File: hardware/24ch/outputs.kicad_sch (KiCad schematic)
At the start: 41 parts, among them J701 TRIP C-NO-NC, J702 ALM C-NO-NC, J703 RS485 A B GND, K701 G6K-2F-Y DC5, K702 G6K-2F-Y DC5, Q701 2N7002, Q702 2N7002, U703 ADM2587EBRWZ

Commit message: 24ch cheaper-parts variant (0036): TMP126, CA-IS3761HW, RS-485 DNP, drop-in swaps
- CJ sensors ADT7310 x6 -> TMP126DCKR (C5219998); R443 22k DIN_ISO-DOUT_ISO for the
  3-wire SIO, R415 removed, ALERT grounded. Sensors moved <= 8 mm to clear spots beside
  their 100 nF (no closer spot to the terminals without touching TC traces, 0035 D2).
- ISO7761 -> CA-IS3761HW (same pinout, 5F/1R, default high); BOCHEN 3296W trimmer;
  SAMWHA 22u 1210.
- RS-485 block DNP: footprints kept; fab.py drops DNP parts from BOM/CPL and writes
  DNP.txt; cost.py skips them. External window watchdog tried and removed (owner).
- gen/delta.py: carry a schematic change onto the routed board (replace/add/remove,
  re-net, DNP, OLD>NEW@DEG reuse); it never deletes another net's track under a pad.
- Board: incremental edits only; analog nets (TC*, V_BIAS, VREF, REF*) identical to
  the pre-0036 board. Gates: ERC 0/0 (471 symbols); fab.py DRC/unconnected/parity
  0/0/0; pincaps 0 over. Parts ~$105 -> ~$72/board (CALCULATIONS 8.1, by hand).
- Docs: decision 0036, CALCULATIONS 8, ISSUES (I-109, I-114, I-119, I-104, I-094,
  new I-123 stock), STATE, 24ch README, superseded.txt.

Co-Authored-By: Claude Opus 5.5 <noreply@anthropic.com>
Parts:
- C731, C732, C733, C734, C735, C736, D731, J703, JP731, JP732, JP733, R733, R734, R735, R736, U703: now not fitted
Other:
- note added: "Isolated RS-485 / Modbus RTU (never in the trip path) - DNP: footprints only, fit when a site needs it (0036)"
- note removed: "Isolated RS-485 / Modbus RTU (never in the trip path)"
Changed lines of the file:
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@@
 		)
 	)
-	(text "Isolated RS-485 / Modbus RTU (never in the trip path)"
+	(text "Isolated RS-485 / Modbus RTU (never in the trip path) - DNP: footprints only, fit when a site needs it (0036)"
 		(exclude_from_sim no)
 		(at 15 119.6124 0)
@@
 		(in_bom yes)
 		(on_board yes)
-		(dnp no)
+		(dnp yes)
 		(property "Reference" "U703"
 			(at 27.94 128.68 0)
@@
 		(in_bom yes)
 		(on_board yes)
-		(dnp no)
+		(dnp yes)
 		(property "Reference" "R733"
 			(at 78.016 141.24 0)
@@
 		(in_bom yes)
 		(on_board yes)
-		(dnp no)
+		(dnp yes)
 		(property "Reference" "C735"
 			(at 114.592 138.7 0)
@@
 		(in_bom yes)
 		(on_board yes)
-		(dnp no)
+		(dnp yes)
 		(property "Reference" "C736"
 			(at 129.832 141.24 0)
@@
 		(in_bom yes)
 		(on_board yes)
-		(dnp no)
+		(dnp yes)
 		(property "Reference" "C731"
 			(at 142.532 138.7 0)
@@
 		(in_bom yes)
 		(on_board yes)
-		(dnp no)
+		(dnp yes)
 		(property "Reference" "C732"
 			(at 157.772 138.7 0)
@@
 		(in_bom yes)
 		(on_board yes)
-		(dnp no)
+		(dnp yes)
 		(property "Reference" "C733"
 			(at 170.472 141.24 0)
@@
 		(in_bom yes)
 		(on_board yes)
-		(dnp no)
+		(dnp yes)
 		(property "Reference" "C734"
 			(at 183.172 141.24 0)
@@
 		(in_bom yes)
 		(on_board yes)
-		(dnp no)
+		(dnp yes)
 		(property "Reference" "D731"
 			(at 201.93 129.95 0)
@@
 		(in_bom yes)
 		(on_board yes)
-		(dnp no)
+		(dnp yes)
 		(property "Reference" "JP731"
 			(at 253.53 126 0)
@@
 		(in_bom yes)
 		(on_board yes)
-		(dnp no)
+		(dnp yes)
 		(property "Reference" "R734"
 			(at 265.976 141.24 0)
@@
 		(in_bom yes)
 		(on_board yes)
-		(dnp no)
+		(dnp yes)
 		(property "Reference" "JP732"
 			(at 296.71 126 0)
@@
 		(in_bom yes)
 		(on_board yes)
-		(dnp no)
+		(dnp yes)
 		(property "Reference" "R735"
 			(at 311.696 141.24 0)
@@
 		(in_bom yes)
 		(on_board yes)
-		(dnp no)
+		(dnp yes)
 		(property "Reference" "JP733"
 			(at 342.43 126 0)
@@
 		(in_bom yes)
 		(on_board yes)
-		(dnp no)
+		(dnp yes)
 		(property "Reference" "R736"
 			(at 354.876 141.24 0)
@@
 		(in_bom yes)
 		(on_board yes)
-		(dnp no)
+		(dnp yes)
 		(property "Reference" "J703"
 			(at 385.61 128.54 0)

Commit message: 24ch 0036 D7/D8: screw terminals face the board edge; supplier files as an RFQ
- J601/J701/J702/J703 turned 180 deg about the middle pin (wire entry was blocked by the
  relays ~2 mm in front); pin numbers 1<->3 swapped in the generator so every position keeps
  its net, label and copper. RS-485 row (DNP) moved 0.5 mm with its track ends, BIAS_B routed
  around J703 pin 1, TRIP_COM stub extended to the round pad.
- delta.py: MPN/LCSC/Manufacturer fields go to F.Fab hidden (were printed on the silkscreen of
  the six TMP126), new footprints hide reference/value like the rest of the board.
- fab.py: ORDER-NOTES rewritten as a friendly request for quotation (LCSC = reference only,
  equivalents welcome, preferences not conditions, terminal direction named); BOM.csv/CPL.csv;
  supplier ACCESSORIES.csv without internal notes or RS-485 items.
- Gates: ERC 0/0; DRC 0 violations / 0 unconnected; pincaps 0 over; analog nets identical to
  the pre-0036 board.

Co-Authored-By: Claude Opus 5.5 <noreply@anthropic.com>
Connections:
- net ALM_COM: now also J702.3 (Pin_3); no longer J702.1 (Pin_1)
- net ALM_NC: now also J702.1 (Pin_1); no longer J702.3 (Pin_3)
- net GND_RS485: now also J703.1 (Pin_1); no longer J703.3 (Pin_3)
- net RS485_A: now also J703.3 (Pin_3); no longer J703.1 (Pin_1)
- net TRIP_COM: now also J701.3 (Pin_3); no longer J701.1 (Pin_1)
- net TRIP_NC: now also J701.1 (Pin_1); no longer J701.3 (Pin_3)
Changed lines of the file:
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@@
 		)
 	)
-	(label "TRIP_COM"
+	(label "TRIP_NC"
 		(at 294.64 27.94 180)
 		(effects
@@
 		)
 	)
-	(label "TRIP_NC"
+	(label "TRIP_COM"
 		(at 294.64 33.02 180)
 		(effects
@@
 		)
 	)
-	(label "ALM_COM"
+	(label "ALM_NC"
 		(at 223.52 78.74 180)
 		(effects
@@
 		)
 	)
-	(label "ALM_NC"
+	(label "ALM_COM"
 		(at 223.52 83.82 180)
 		(effects
@@
 		)
 	)
-	(label "RS485_A"
+	(label "GND_RS485"
 		(at 375.92 127 180)
 		(effects
@@
 		)
 	)
-	(label "GND_RS485"
+	(label "RS485_A"
 		(at 375.92 132.08 180)
 		(effects

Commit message: 24ch 0036 D9: RS-485/Modbus fitted again (owner), release tooling for no DNP
- c_out.py: the 16 RS-485 parts are fitted (reverses 0036 D2); build.py
  ERC 0/0, netlist check 0/0. delta.py cleared the 16 DNP flags on the
  board, no copper changed (0 tracks deleted); pincaps 0 over the limit.
- fab.py: DNP.txt says "none" when every footprint is fitted; jumper shunts
  for JP731-JP733 go to the supplier accessories; J703 in the terminal
  orientation note.
- assembly_spec.py: counts and the through-hole list read from BOM.csv;
  section 6 adapts to a release without DNP; U703 and J703 in the checklist.
- docs: 0036 D9, I-094, CALCULATIONS 8.1 (+$8.64/board).

Co-Authored-By: Claude Opus 5.5 <noreply@anthropic.com>
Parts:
- C731, C732, C733, C734, C735, C736, D731, J703, JP731, JP732, JP733, R733, R734, R735, R736, U703: now fitted
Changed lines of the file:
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@@
 		(in_bom yes)
 		(on_board yes)
-		(dnp yes)
+		(dnp no)
 		(property "Reference" "U703"
 			(at 27.94 128.68 0)
@@
 		(in_bom yes)
 		(on_board yes)
-		(dnp yes)
+		(dnp no)
 		(property "Reference" "R733"
 			(at 78.016 141.24 0)
@@
 		(in_bom yes)
 		(on_board yes)
-		(dnp yes)
+		(dnp no)
 		(property "Reference" "C735"
 			(at 114.592 138.7 0)
@@
 		(in_bom yes)
 		(on_board yes)
-		(dnp yes)
+		(dnp no)
 		(property "Reference" "C736"
 			(at 129.832 141.24 0)
@@
 		(in_bom yes)
 		(on_board yes)
-		(dnp yes)
+		(dnp no)
 		(property "Reference" "C731"
 			(at 142.532 138.7 0)
@@
 		(in_bom yes)
 		(on_board yes)
-		(dnp yes)
+		(dnp no)
 		(property "Reference" "C732"
 			(at 157.772 138.7 0)
@@
 		(in_bom yes)
 		(on_board yes)
-		(dnp yes)
+		(dnp no)
 		(property "Reference" "C733"
 			(at 170.472 141.24 0)
@@
 		(in_bom yes)
 		(on_board yes)
-		(dnp yes)
+		(dnp no)
 		(property "Reference" "C734"
 			(at 183.172 141.24 0)
@@
 		(in_bom yes)
 		(on_board yes)
-		(dnp yes)
+		(dnp no)
 		(property "Reference" "D731"
 			(at 201.93 129.95 0)
@@
 		(in_bom yes)
 		(on_board yes)
-		(dnp yes)
+		(dnp no)
 		(property "Reference" "JP731"
 			(at 253.53 126 0)
@@
 		(in_bom yes)
 		(on_board yes)
-		(dnp yes)
+		(dnp no)
 		(property "Reference" "R734"
 			(at 265.976 141.24 0)
@@
 		(in_bom yes)
 		(on_board yes)
-		(dnp yes)
+		(dnp no)
 		(property "Reference" "JP732"
 			(at 296.71 126 0)
@@
 		(in_bom yes)
 		(on_board yes)
-		(dnp yes)
+		(dnp no)
 		(property "Reference" "R735"
 			(at 311.696 141.24 0)
@@
 		(in_bom yes)
 		(on_board yes)
-		(dnp yes)
+		(dnp no)
 		(property "Reference" "JP733"
 			(at 342.43 126 0)
@@
 		(in_bom yes)
 		(on_board yes)
-		(dnp yes)
+		(dnp no)
 		(property "Reference" "R736"
 			(at 354.876 141.24 0)
@@
 		(in_bom yes)
 		(on_board yes)
-		(dnp yes)
+		(dnp no)
 		(property "Reference" "J703"
 			(at 385.61 128.54 0)

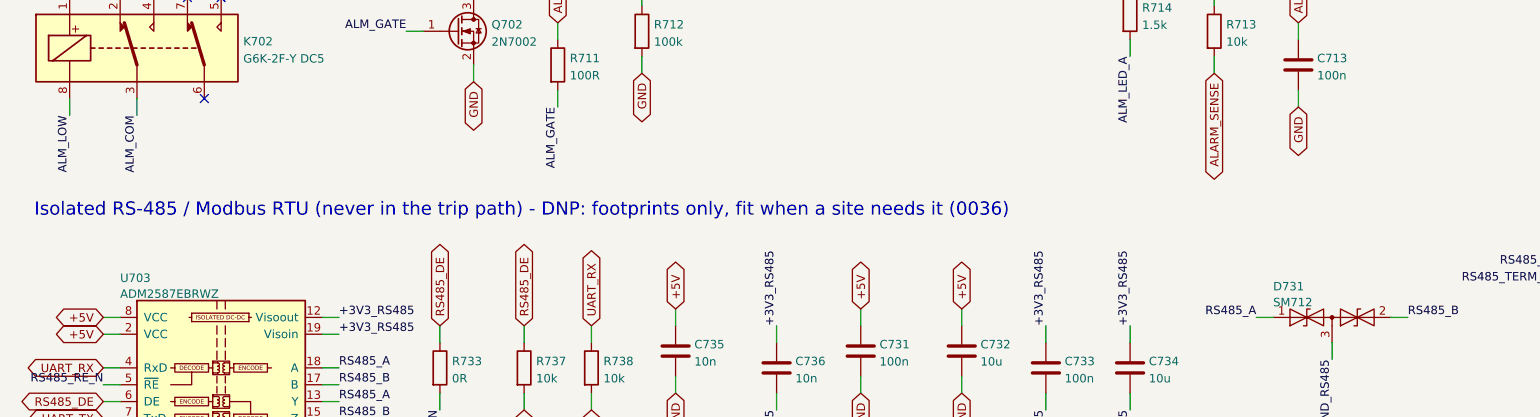
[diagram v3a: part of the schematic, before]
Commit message: 24ch REV A4: Astra review fixes, release 195548-b4c4e2
Astra (gpt-6-astra, high): no redesign blocker. Fixed its documentation
findings: schematic title REV A4 and RS-485 block no longer called DNP;
ASSEMBLY-SPEC.pdf generated into the release; I-085 now says J601 pin 1 =
CHASSIS, pin 3 = +24V (0036 D7 turn); TMP126 write transactions keep
SIO_WR_N low through data and CRC (0041, c_iso.py note).
ERC 0/0, netlist 0 mismatches, board unchanged (delta dry: 0), release DRC
0/0/0, BOM 96 lines. Previous releases archived in _OLD_DO_NOT_ORDER.

Co-Authored-By: Claude Opus 5.5 <noreply@anthropic.com>
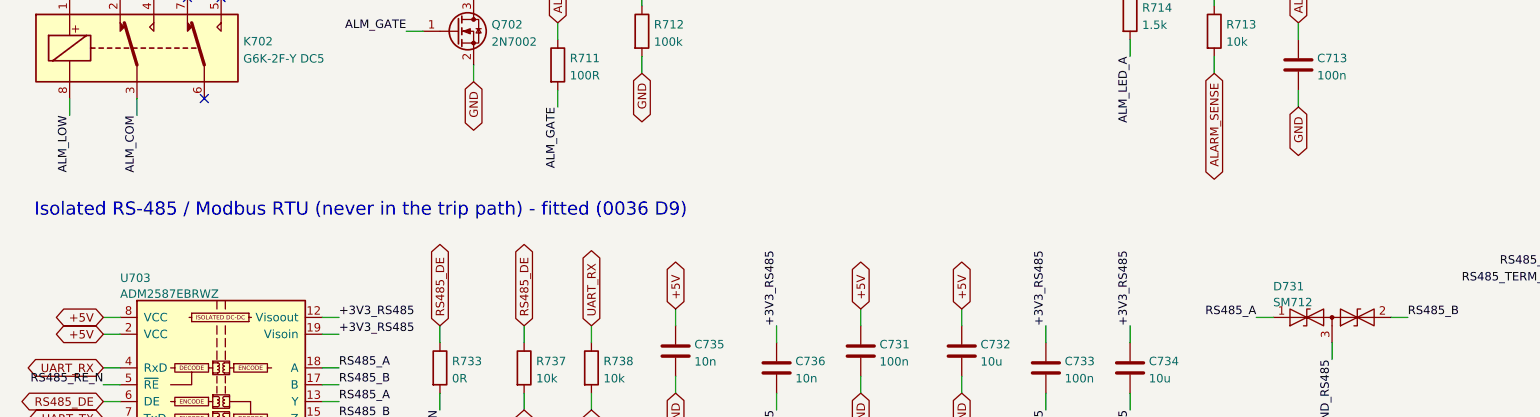
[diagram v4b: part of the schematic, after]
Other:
- note added: "Isolated RS-485 / Modbus RTU (never in the trip path) - fitted (0036 D9)"
- note removed: "Isolated RS-485 / Modbus RTU (never in the trip path) - DNP: footprints only, fit when a site needs it (0036)"
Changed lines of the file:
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@@
 		)
 	)
-	(text "Isolated RS-485 / Modbus RTU (never in the trip path) - DNP: footprints only, fit when a site needs it (0036)"
+	(text "Isolated RS-485 / Modbus RTU (never in the trip path) - fitted (0036 D9)"
 		(exclude_from_sim no)
 		(at 15 119.6124 0)
